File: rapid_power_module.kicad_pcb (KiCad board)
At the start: 2 copper layers, 110.8 x 136 mm, 184 parts, among them J1 Conn_02x04_Top_Bottom, J11 SWD Header, J12 SWD Header, J16 USB_C_Receptacle_USB2.0, J17 TC2050, J3 Conn_02x04_Top_Bottom, J5 Molex MicroFit 2x2, J6 Molex MicroFit 2x2, J7 Molex MicroFit 2x2, J8 Molex MicroFit 2x2, J9 Molex MicroFit 2x2, Q5 NMOS, Q6 NMOS, Q7 NMOS, Q8 NMOS, SW1 KMR721NGLFS, SW2 KMR721NGLFS, U1 BQ25756RRVR, U10 L7805, U11 MCP2562-E-SN, U12 STM32F105RCTx, U13 AZ1117I-3.3, U14 TPD4E1U06, U15 TPD4E1U06, U2 CYPD3177-24LQ, U3 BQ76952PFBR, Y3 8MHz 12pF

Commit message: rough component placement
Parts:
- added J2: Conn_02x03_Odd_Even, Connector_PinHeader_1.00mm:PinHeader_2x03_P1.00mm_Vertical, B.Cu at (170.0, 32.4)
- added J4: Conn_02x03_Odd_Even, Connector_PinHeader_1.00mm:PinHeader_2x03_P1.00mm_Vertical, B.Cu at (166.0, 32.2)
- added R1: 2.4, Resistor_SMD:R_0603_1608Metric, F.Cu at (134.7, 84.6)
- C23: footprint Capacitor_SMD:C_0402_1005Metric -> Capacitor_SMD:C_0805_2012Metric
- C59: footprint Capacitor_SMD:C_0402_1005Metric -> Capacitor_SMD:C_0603_1608Metric
- C61, C80: footprint Capacitor_SMD:C_1206_3216Metric -> Capacitor_SMD:C_0603_1608Metric
- J1, J11, J12, J3, J5, J6, L2: moved to B.Cu
- J16: moved to F.Cu
- R11, R12, R2, R20, R21: footprint Resistor_SMD:R_2512_6332Metric -> Resistor_SMD:R_0603_1608Metric
- R26, R45, R73, R74, R75, R76, R86, R87, R88, R89, R90, R92, R93: footprint Resistor_SMD:R_0402_1005Metric -> Resistor_SMD:R_0603_1608Metric
- moved F3 140.9 mm to (135.0, 49.2), turned to 0 degrees
- moved F1 136.2 mm to (135.0, 38.0), turned to 180 degrees
- moved C62 134.1 mm to (158.6, 68.3)
- moved C61 133.5 mm to (158.2, 63.0)
- moved C80 132.8 mm to (158.2, 60.5)
- moved C60 129.7 mm to (172.0, 48.2)
- moved C58 129.6 mm to (172.0, 50.5)
- moved J3 123.6 mm to (139.0, 147.5), turned to 0 degrees
- moved C45 120.3 mm to (134.8, 101.2), turned to 90 degrees
- moved C46 120.3 mm to (139.6, 97.7), turned to 45 degrees
- moved J1 119.5 mm to (156.6, 147.7), turned to 0 degrees
- moved C47 117.6 mm to (142.2, 91.5)
- moved C48 117.1 mm to (142.2, 93.1)
- moved R76 116.2 mm to (141.8, 32.0), turned to 90 degrees
- moved C49 112.3 mm to (140.6, 88.9)
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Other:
- board size 110.8 x 136 mm -> 80 x 136 mm
- copper layers 2 -> 4
- board text added: "BOOT"
- board text added: "RST"

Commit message: some placement changes
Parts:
- moved H3 1.21 mm to (99.0, 141.0)
- moved H2 0.76 mm to (171.0, 26.0)
- moved H4 0.71 mm to (171.0, 141.0)
- moved H1 0.64 mm to (99.0, 26.0)
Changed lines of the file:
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@@
 			(psa4output no)
 			(plot_black_and_white yes)
+			(plotinvisibletext no)
 			(sketchpadsonfab no)
 			(plotpadnumbers no)
@@
 	(footprint "MountingHole:MountingHole_3.2mm_M3_Pad_Via"
 		(layer "F.Cu")
-		(at 170.5 141.5)
+		(at 171 141)
 		(descr "Mounting Hole 3.2mm, M3, generated by kicad-footprint-generator mountinghole.py")
 		(tags "mountinghole M3")
@@
 			(at 0 1.43 0)
 			(layer "F.Fab")
+			(hide yes)
 			(effects
 				(font
@@
 			(at 0 1.43 0)
 			(layer "F.Fab")
+			(hide yes)
 			(effects
 				(font
@@
 			(at 0 1.43 90)
 			(layer "F.Fab")
+			(hide yes)
 			(effects
 				(font
@@
 			(at 0 1.43 0)
 			(layer "F.Fab")
+			(hide yes)
 			(effects
 				(font
@@
 			(at 0 1.43 0)
 			(layer "F.Fab")
+			(hide yes)
 			(effects
 				(font
@@
 			(at 0 1.43 0)
 			(layer "F.Fab")
+			(hide yes)
 			(effects
 				(font
@@
 			(at 0 1.679999 90)
 			(layer "F.Fab")
+			(hide yes)
 			(effects
 				(font
@@
 			(at 0 1.43 90)
 			(layer "F.Fab")
+			(hide yes)
 			(effects
 				(font
@@
 			(at 0 1.43 0)
 			(layer "F.Fab")
+			(hide yes)
 			(effects
 				(font
@@
 			(at 0 1.43 0)
 			(layer "F.Fab")
+			(hide yes)
 			(effects
 				(font
@@
 			(at 0 1.43 45)
 			(layer "F.Fab")
+			(hide yes)
 			(effects
 				(font
@@
 			(at 0 2.63 0)
 			(layer "F.Fab")
+			(hide yes)
 			(effects
 				(font
@@
 			(at 0 1.679999 90)
 			(layer "F.Fab")
+			(hide yes)
 			(effects
 				(font
@@
 			(at 0 1.43 0)
 			(layer "F.Fab")
+			(hide yes)
 			(effects
 				(font
@@
 			(at 0 1.43 90)
 			(layer "F.Fab")
+			(hide yes)
 			(effects
 				(font
@@
 			(at 0 1.679999 0)
 			(layer "F.Fab")
+			(hide yes)
 			(effects
 				(font
@@
 			(at 0 1.43 90)
 			(layer "F.Fab")
+			(hide yes)
 			(effects
 				(font
@@
 			(at 0 1.679999 0)
 			(layer "F.Fab")
+			(hide yes)
 			(effects
 				(font
@@
 			(at 0 1.43 0)
 			(layer "F.Fab")
+			(hide yes)
 			(effects
 				(font
@@
 			(at 0 1.43 0)
 			(layer "F.Fab")
+			(hide yes)
 			(effects
 				(font
@@
 	(footprint "MountingHole:MountingHole_3.2mm_M3_Pad_Via"
 		(layer "F.Cu")
-		(at 100.1 141.5)
+		(at 99 141)
 		(descr "Mounting Hole 3.2mm, M3, generated by kicad-footprint-generator mountinghole.py")
 		(tags "mountinghole M3")
@@
 			(at 0 1.43 0)
 			(layer "F.Fab")
+			(hide yes)
 			(effects
 				(font
@@
 			(at 0 3.330001 0)
 			(layer "F.Fab")
+			(hide yes)
 			(effects
 				(font
@@
 			(at 0 5.85 90)
 			(layer "F.Fab")
+			(hide yes)
 			(effects
 				(font
@@
 			(at 0 1.43 90)
 			(layer "F.Fab")
+			(hide yes)
 			(effects
 				(font
@@
 			(at 0 1.43 90)
 			(layer "F.Fab")
+			(hide yes)
 			(effects
 				(font
@@
 			(at 0 1.43 0)
 			(layer "F.Fab")
+			(hide yes)
 			(effects
 				(font
@@
 			(at 0 1.43 90)
 			(layer "F.Fab")
+			(hide yes)
 			(effects
 				(font
@@
 			(at 0 1.43 90)
 			(layer "F.Fab")
+			(hide yes)
 			(effects
 				(font
@@
 			(at 0 1.65 0)
 			(layer "F.Fab")
+			(hide yes)
 			(effects
 				(font
@@
 			(at 0 1.43 90)
 			(layer "F.Fab")
+			(hide yes)
 			(effects
 				(font
@@
 			(at 0 1.43 45)
 			(layer "F.Fab")
+			(hide yes)
 			(effects
 				(font
@@
 			(at 0 1.43 0)
 			(layer "F.Fab")
+			(hide yes)
 			(effects
 				(font
@@
 			(at 0 4.329999 0)
 			(layer "F.Fab")
+			(hide yes)
 			(effects
 				(font
@@
 			(at 0 2.63 0)
 			(layer "F.Fab")
+			(hide yes)
 			(effects
 				(font
@@
 			(at 0 1.43 0)
 			(layer "F.Fab")
+			(hide yes)
 			(effects
 				(font
@@
 			(at 0 1.43 0)
 			(layer "F.Fab")
+			(hide yes)
 			(effects
 				(font
@@
 			(at 0 1.43 45)
 			(layer "F.Fab")
+			(hide yes)
 			(effects
 				(font
@@
 			(at 0 1.43 0)
 			(layer "F.Fab")
+			(hide yes)
 			(effects
 				(font
@@
 			(at 0 1.43 90)
 			(layer "F.Fab")
+			(hide yes)
 			(effects
 				(font
@@
 			(at 0 1.43 90)
 			(layer "F.Fab")
+			(hide yes)
 			(effects
 				(font
@@
 			(at 0 1.43 0)
 			(layer "F.Fab")
+			(hide yes)
 			(effects
 				(font
@@
 			(at 0 1.43 0)
 			(layer "F.Fab")
+			(hide yes)
 			(effects
 				(font
@@
 			(at 0 1.43 0)
 			(layer "F.Fab")
+			(hide yes)
 			(effects
 				(font
@@
 			(at 0 1.43 0)
 			(layer "F.Fab")
+			(hide yes)
 			(effects
 				(font
@@
 			(at 0 1.43 0)
 			(layer "F.Fab")
+			(hide yes)
 			(effects
 				(font
@@
 			(at 0 1.43 0)
 			(layer "F.Fab")
+			(hide yes)
 			(effects
 				(font
@@
 			(at 0 1.43 90)
 			(layer "F.Fab")
+			(hide yes)
 			(effects
 				(font
@@
 			(at 0 1.43 0)
 			(layer "F.Fab")
+			(hide yes)
 			(effects
 				(font
@@
 			(at 0 1.43 0)
 			(layer "F.Fab")
+			(hide yes)
 			(effects
 				(font
@@
 			(at 0 1.55 0)
 			(layer "F.Fab")
+			(hide yes)
 			(effects
 				(font
@@
 			(at 0 1.43 0)
 			(layer "F.Fab")
+			(hide yes)
 			(effects
 				(font
@@
 			(at 0 1.43 0)
 			(layer "F.Fab")
+			(hide yes)
 			(effects
 				(font
@@
 			(at 0 1.43 90)
 			(layer "F.Fab")
+			(hide yes)
 			(effects
 				(font
@@
 			(at 0 1.43 90)
 			(layer "F.Fab")
+			(hide yes)
 			(effects
 				(font
@@
 			(at 0 1.43 0)
 			(layer "F.Fab")
+			(hide yes)
 			(effects
 				(font
@@
 			(at 0 1.43 90)
 			(layer "F.Fab")
+			(hide yes)
 			(effects
 				(font
@@
 			(at 0 1.43 0)
 			(layer "F.Fab")
+			(hide yes)
 			(effects
 				(font
@@
 			(at 0 1.85 0)
 			(layer "F.Fab")
+			(hide yes)
 			(effects
 				(font
@@
 			(at 0 1.43 90)
 			(layer "F.Fab")
+			(hide yes)
 			(effects
 				(font
@@
 	(footprint "MountingHole:MountingHole_3.2mm_M3_Pad_Via"
 		(layer "F.Cu")
-		(at 99.4 26.5)
+		(at 99 26)
 		(descr "Mounting Hole 3.2mm, M3, generated by kicad-footprint-generator mountinghole.py")
 		(tags "mountinghole M3")
@@
 			(at 0 1.43 0)
 			(layer "F.Fab")
+			(hide yes)
 			(effects
 				(font
@@
 			(at 0 1.43 0)
 			(layer "F.Fab")
+			(hide yes)
 			(effects
 				(font
@@
 	(footprint "MountingHole:MountingHole_3.2mm_M3_Pad_Via"
 		(layer "F.Cu")
-		(at 170.302944 26.302944)
+		(at 171 26)
 		(descr "Mounting Hole 3.2mm, M3, generated by kicad-footprint-generator mountinghole.py")
 		(tags "mountinghole M3")
@@
 			(at 0 4.15 0)
 			(layer "F.Fab")
+			(hide yes)
 			(effects
 				(font

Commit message: more routing work
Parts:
- added TP2: TP_CAN_TX, TestPoint:TestPoint_Pad_D1.0mm, F.Cu at (113.8, 42.8)
- added TP3: TP_CAN_RX, TestPoint:TestPoint_Pad_D1.0mm, F.Cu at (114.0, 51.2)
- added TP4: TP_USB_D+, TestPoint:TestPoint_Pad_D1.0mm, F.Cu at (133.2, 37.2)
- added TP5: TP_USB_D-, TestPoint:TestPoint_Pad_D1.0mm, F.Cu at (138.8, 37.2)
- added TP6: TP_USB_CC2, TestPoint:TestPoint_Pad_D1.0mm, F.Cu at (130.2, 31.8)
- added TP7: TP_USB_CC1, TestPoint:TestPoint_Pad_D1.0mm, F.Cu at (139.8, 31.8)
- C10, C23, C9: footprint Capacitor_SMD:C_0805_2012Metric -> Capacitor_SMD:C_0402_1005Metric
- C11: footprint Capacitor_SMD:C_0805_2012Metric -> Resistor_SMD:R_0402_1005Metric
- C12, C13: footprint Capacitor_SMD:C_0603_1608Metric -> Resistor_SMD:R_0402_1005Metric
- C59, C65: footprint Capacitor_SMD:C_0603_1608Metric -> Capacitor_SMD:C_0402_1005Metric
- C61, C80: footprint Capacitor_SMD:C_0603_1608Metric -> Capacitor_SMD:C_1206_3216Metric
- Q5, Q6, Q7, Q8: moved to B.Cu
- R10, R13, R18, R19, R26, R4, R45, R5, R6, R7, R73, R74, R75, R76, R86, R87, R88, R89, R9, R90, R92, R93: footprint Resistor_SMD:R_0603_1608Metric -> Resistor_SMD:R_0402_1005Metric
- R11, R12, R2, R20, R21: footprint Resistor_SMD:R_0603_1608Metric -> Resistor_SMD:R_2512_6332Metric
- moved F1 97.3 mm to (134.9, 135.3)
- moved R83 78.9 mm to (159.1, 24.7), turned to 0 degrees
- moved F3 75.6 mm to (135.0, 124.9), turned to 180 degrees
- moved J11 72.5 mm to (98.8, 47.2), turned to 0 degrees
- moved J12 67.5 mm to (104.2, 47.5), turned to 0 degrees
- moved Q7 66.6 mm to (185.0, 43.2), turned to 180 degrees
- moved Q8 62.5 mm to (185.8, 35.6), turned to 180 degrees
- moved R69 57.6 mm to (121.8, 33.2), turned to 90 degrees
- moved R66 53.7 mm to (102.0, 45.9), turned to -90 degrees
- moved Q5 46.3 mm to (167.0, 36.0), turned to 180 degrees
- moved Q6 43.8 mm to (156.2, 40.0), turned to 180 degrees
- moved C3 29.3 mm to (121.6, 78.5), turned to -90 degrees
- moved R91 28.3 mm to (129.2, 71.5), turned to -90 degrees
- moved L2 27.8 mm to (134.9, 40.6)
- moved C5 27.2 mm to (123.2, 78.5), turned to -90 degrees
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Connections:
- D21 pad 2: STAT1 -> STAT2
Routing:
- net (no net): track 0.00 -> 145.4 mm, vias 0 -> 1
- net Net-(J5-Pin_3): track 0.00 -> 76.5 mm
- net PACK+: track 0.00 -> 71.9 mm
- net ISNK_COARSE: track 0.00 -> 17.3 mm
- net ISNK_FINE: track 0.00 -> 13.3 mm
- net /D0+: track 0.00 -> 13.2 mm, vias 0 -> 2
- net /D0-: track 0.00 -> 12.9 mm, vias 0 -> 2
- net 3.3V PD: track 0.00 -> 12.1 mm
- net USB_D+: track 0.00 -> 8.27 mm
- net PG: track 0.00 -> 7.91 mm
- net USB_D-: track 0.00 -> 7.68 mm
- net I2C_SCL: track 0.00 -> 5.99 mm
- net I2C_SDA: track 0.00 -> 5.78 mm
- net CE: track 0.00 -> 5.54 mm
- net STAT2: track 0.00 -> 4.95 mm
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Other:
- board text added: "+"
- board text added: "-"
- board text added: "BAT 1"
- board text added: "BAT 2"
- board text added: "BAT 3"
- board text added: "EN"
- board text added: "SYS fuse"
- board text added: "VB fuse"

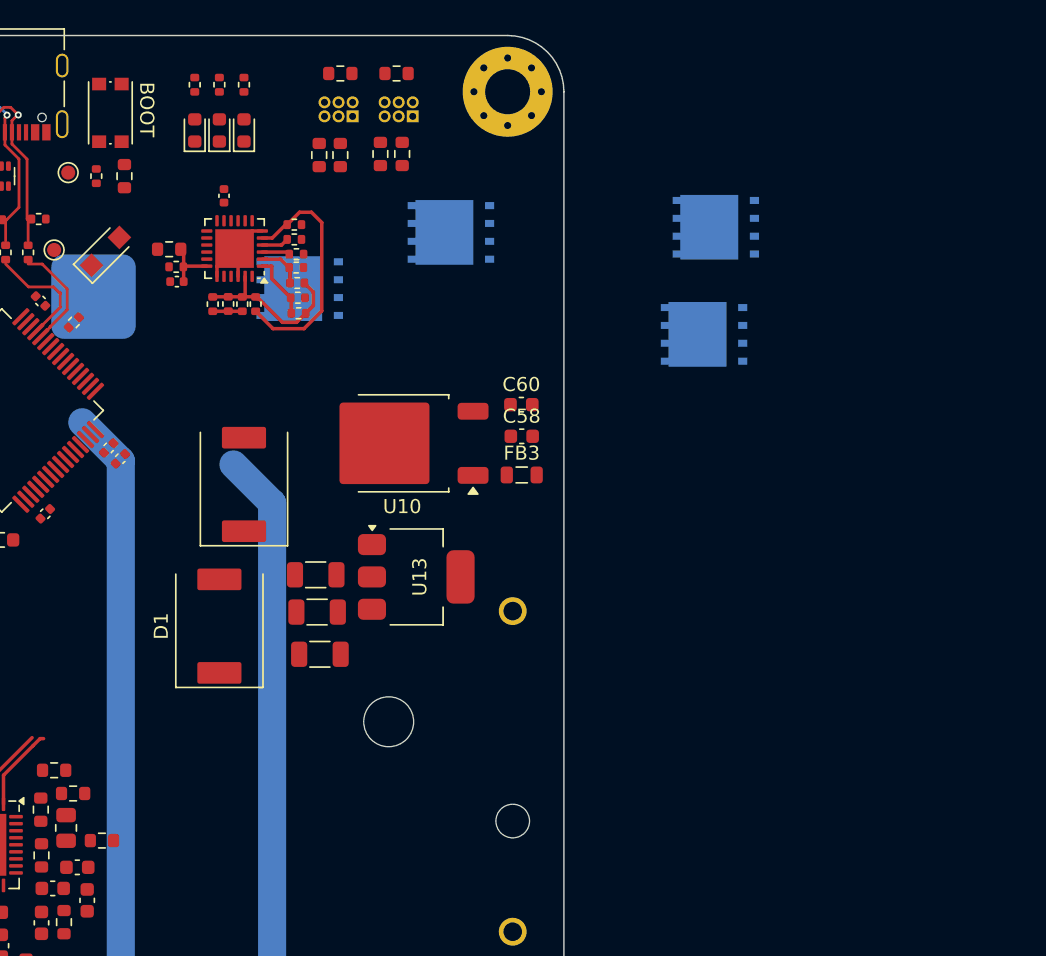
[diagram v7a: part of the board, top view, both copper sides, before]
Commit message: Added Footprints for MOSFETs
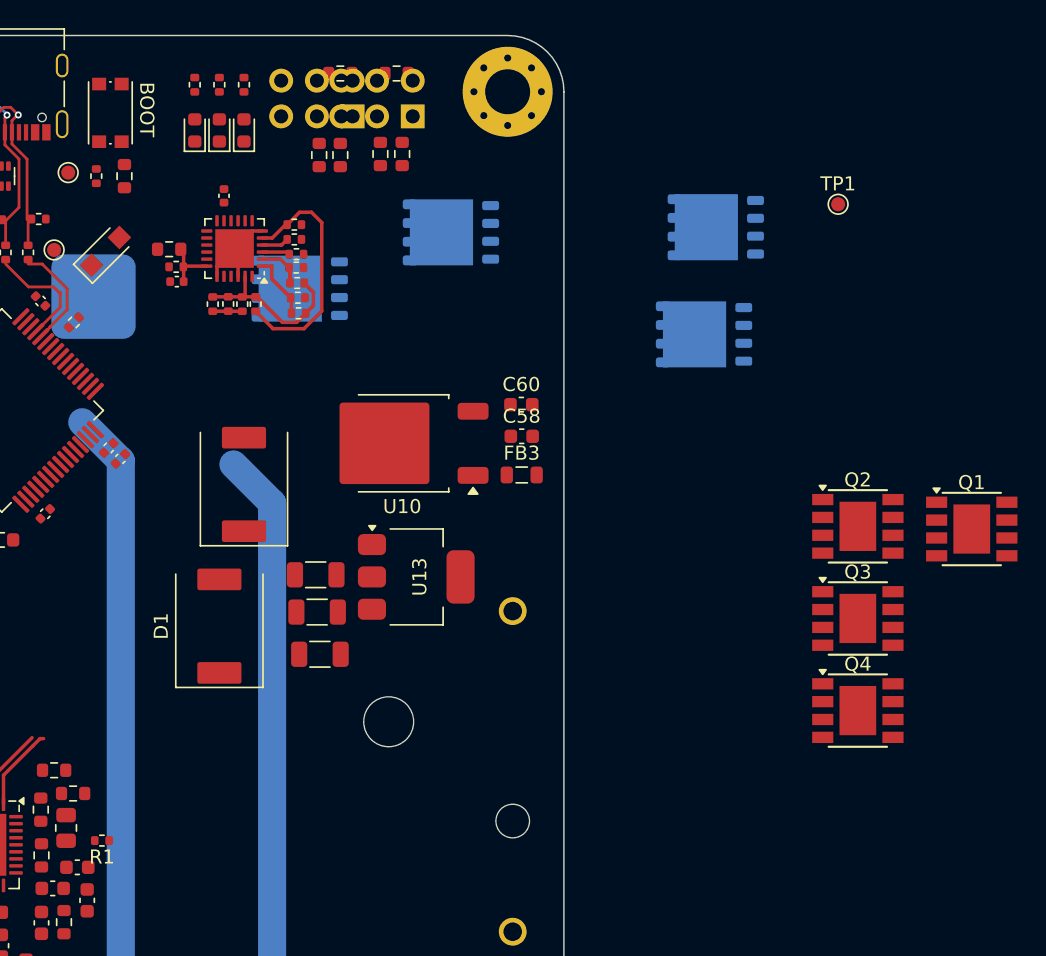
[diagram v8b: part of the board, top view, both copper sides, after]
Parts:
- added Q1: Q_PMOS, Package_SO:Diodes_SO-8EP, F.Cu at (204.0, 57.1)
- added Q2: Q_PMOS, Package_SO:Diodes_SO-8EP, F.Cu at (195.9, 56.9)
- added Q3: Q_PMOS, Package_SO:Diodes_SO-8EP, F.Cu at (195.9, 63.5)
- added Q4: Q_PMOS, Package_SO:Diodes_SO-8EP, F.Cu at (195.9, 70.0)
- added TP1: BuckBoostOut, TestPoint:TestPoint_Pad_D1.0mm, F.Cu at (194.5, 34.0)
- J2, J4: footprint Connector_PinHeader_1.00mm:PinHeader_2x03_P1.00mm_Vertical -> Connector_PinHeader_2.54mm:PinHeader_2x03_P2.54mm_Vertical
- Q5, Q6, Q7, Q8: footprint Package_DFN_QFN:AO_DFN-8-1EP_5.55x5.2mm_P1.27mm_EP4.12x4.6mm -> Package_SON:Infineon_PG-TDSON-8_6.15x5.15mm
- R1: footprint Resistor_SMD:R_0603_1608Metric -> Resistor_SMD:R_0402_1005Metric
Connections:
- U3 pad 41: BAL_LD -> ISNK_FINE
